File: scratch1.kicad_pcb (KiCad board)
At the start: 2 copper layers, 24 parts, among them J1 USB_B_Micro, SW1 SW_Push, U1 ATmega32U4-A, Y1 16MHz

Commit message: finished routing
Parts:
- MX1, MX2, MX3, MX4: footprint MX_Only:MXOnly-1U-NoLED -> MX_Only:MXOnly-1U-Hotswap
- moved C4 11.1 mm to (81.8, 76.4), turned to -90 degrees
- moved C5 10.3 mm to (92.1, 76.4), turned to -90 degrees
- moved J1 1.59 mm to (94.5, 47.6)
- moved R4 0.68 mm to (77.8, 61.0)
- moved Y1 0.15 mm to (87.3, 76.5), turned to 90 degrees
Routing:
- net GND: track 0.00 -> 83.5 mm, vias 0 -> 5
- net COL0: track 0.00 -> 73.4 mm, vias 0 -> 4
- net COL1: track 0.00 -> 68.3 mm, vias 0 -> 4
- net ROW0: track 0.00 -> 45.2 mm, vias 0 -> 3
- net ROW1: track 0.00 -> 25.8 mm
- net +5V: track 0.00 -> 20.5 mm
- net Net-(U1-~{RESET}): track 0.00 -> 15.4 mm
- net VCC: track 0.00 -> 14.7 mm
- net Net-(U1-XTAL1): track 0.00 -> 11.7 mm
- net Net-(U1-XTAL2): track 0.00 -> 11.1 mm
- net D+: track 0.00 -> 9.49 mm
- net Net-(U1-D-): track 0.00 -> 8.27 mm
- net D-: track 0.00 -> 5.03 mm
- net Net-(D4-A): track 0.00 -> 4.92 mm
- net Net-(D2-A): track 0.00 -> 4.92 mm
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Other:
- board outline added: 63.5 x 39.7 mm

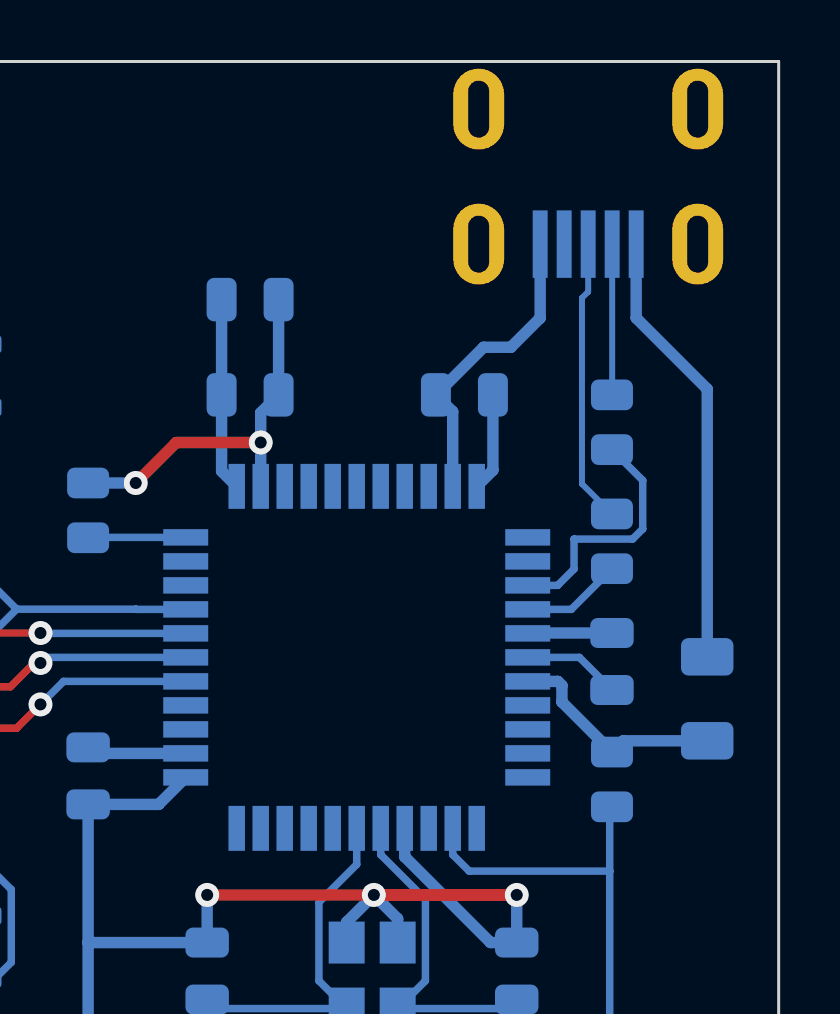
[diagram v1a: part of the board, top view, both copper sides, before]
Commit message: connector updated, but MX footprint to be also updated
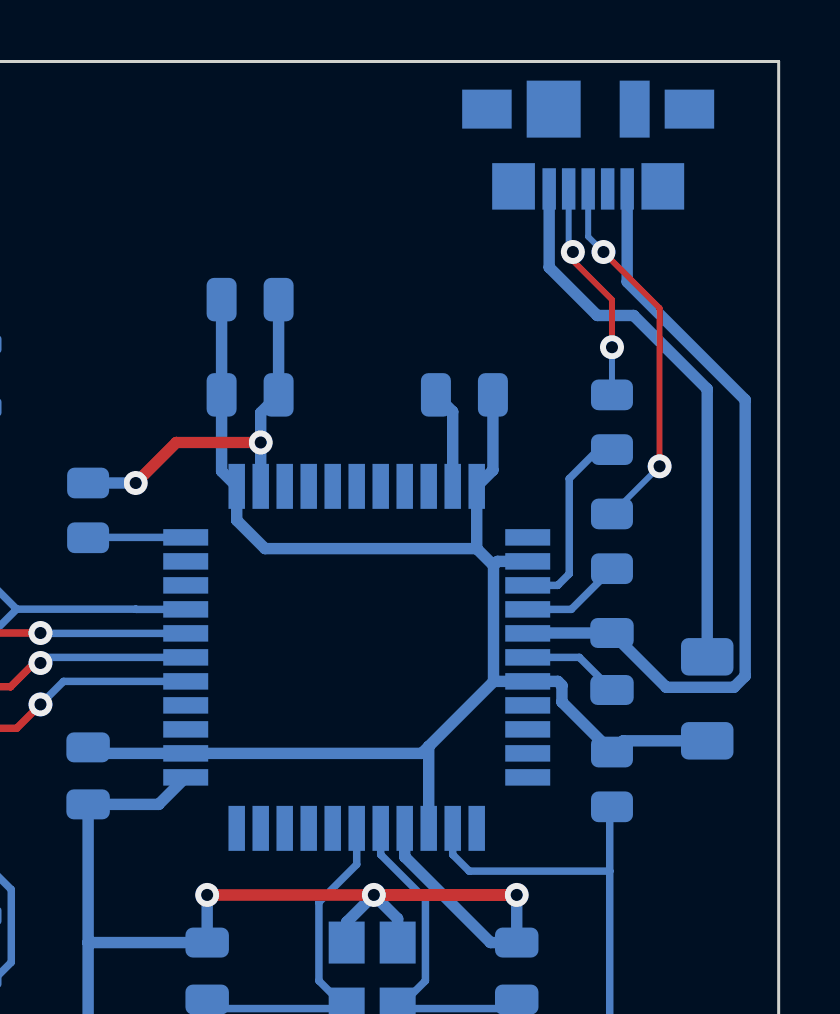
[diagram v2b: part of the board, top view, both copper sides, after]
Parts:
- J1: footprint random-keyboard-parts:Molex-0548190589 -> Connector_USB:USB_Micro-B_Molex_47346-0001
- moved J1 1.20 mm to (94.5, 48.8), turned to 0 degrees
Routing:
- net +5V: track 20.5 -> 53.1 mm
- net GND: track 83.5 -> 99.7 mm
- net VCC: track 14.7 -> 18.5 mm
- net D+: track 9.49 -> 12.5 mm, vias 0 -> 2
- net D-: track 5.03 -> 7.47 mm, vias 0 -> 2
- net Net-(U1-D-): track 8.27 -> 6.54 mm

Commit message: error solved
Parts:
- MX1, MX2, MX3, MX4: footprint MX_Only:MXOnly-1U-Hotswap -> MX_Only:MXOnly-1U-Hotswap-nowrap
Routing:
- net GND: track 99.7 -> 131.8 mm, vias 5 -> 11
- net +5V: track 53.1 -> 56.1 mm
